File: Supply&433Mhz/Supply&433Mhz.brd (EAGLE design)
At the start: 65.1 x 56.5 mm, 17 parts, among them K1 61004021821, P1 DF11-06-2DSA, Q1 BS170

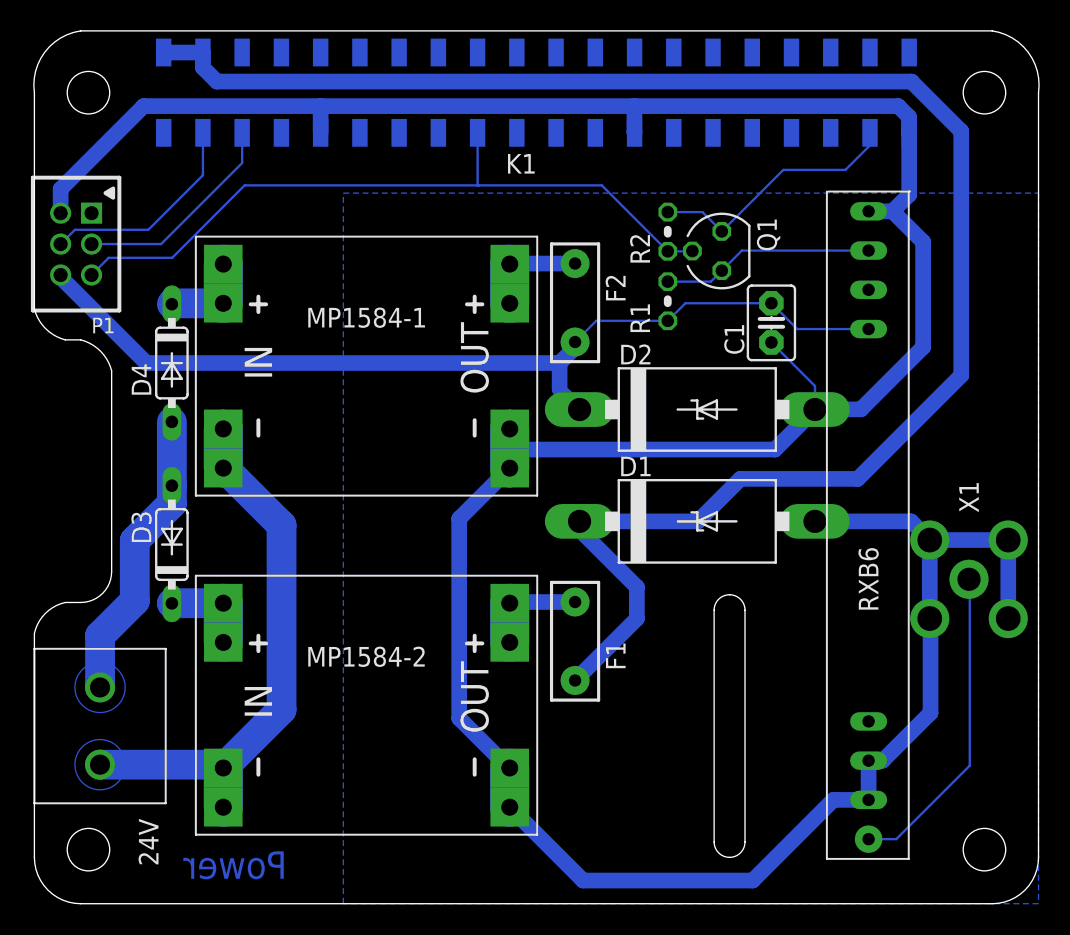
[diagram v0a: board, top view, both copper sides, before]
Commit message: Change connector positions and drills.
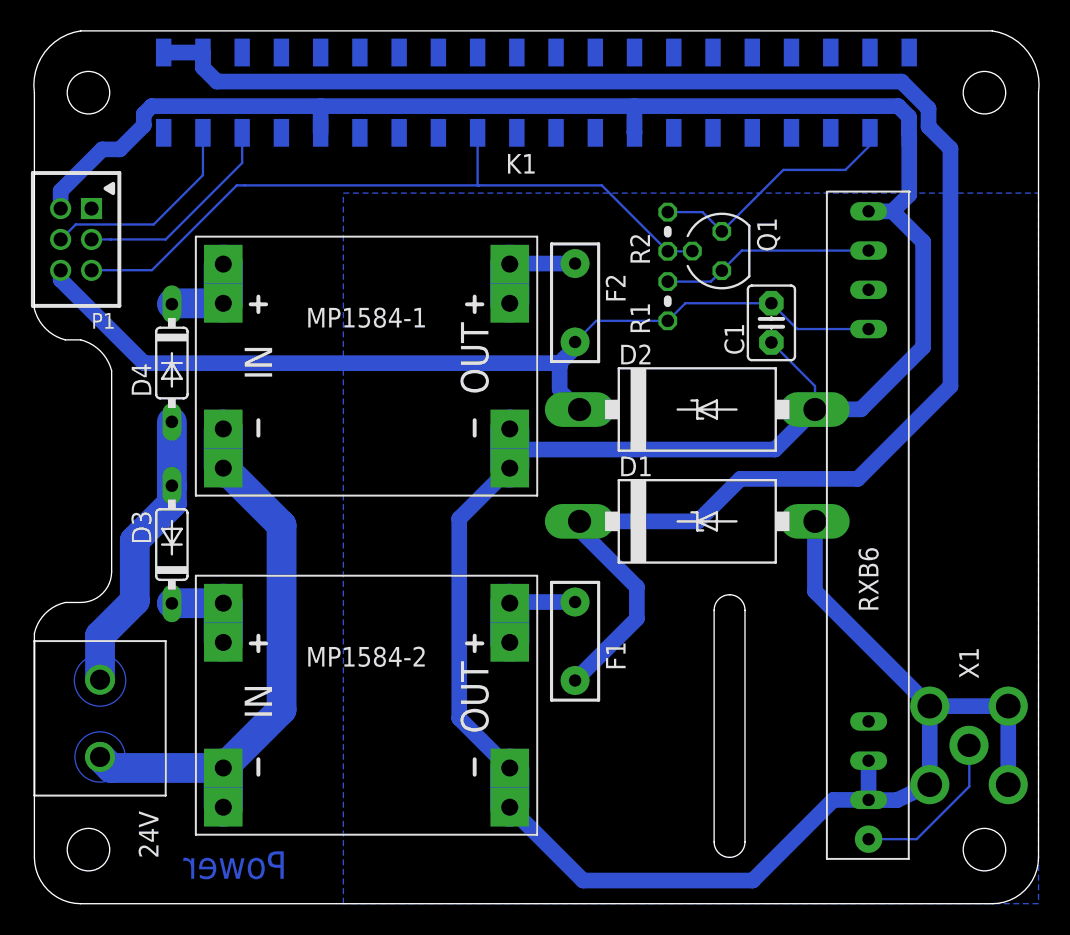
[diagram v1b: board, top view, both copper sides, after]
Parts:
- moved X1 10.8 mm to (60.5, 10.2)
- moved 24V 0.50 mm to (4.25, 12.0)
- moved P1 0.30 mm to (2.70, 43.0)
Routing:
- net N$8: track 21.5 -> 10.6 mm
- net N$5: track 112.3 -> 111.3 mm
- net GND: track 207.8 -> 206.8 mm
- net AGND: track 35.7 -> 36.2 mm
- net +24V: track 19.1 -> 18.6 mm
